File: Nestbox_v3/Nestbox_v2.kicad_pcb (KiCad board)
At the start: 2 copper layers, 85 x 60 mm, 125 parts, among them CON301 Micro_SD_Card, J201 BATT_CONN_01X02, J401 LB_DETECT_CONN_01X04, J402 CONN_01X05, J501 CONN_01X01, J502 CONN_01X06, J601 LOAD_CELL_CONN_01X04, J701 RFID_CONN_01X05, P301 RX/TX, P302 TST/RST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

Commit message: removed unnecessary footprints from PCB
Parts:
- removed CON301: Micro_SD_Card, Octanis3:MICRO-SD9+4P-SMD-16.1X14.5X1.85MM
- removed J401: LB_DETECT_CONN_01X04, Terminal_Blocks:TerminalBlock_Pheonix_MPT-2.54mm_4pol
- removed J501: CONN_01X01, Pin_Headers:Pin_Header_Straight_1x01_Pitch2.54mm
- removed JP701: V_RFID_Jumper_SELECT_Dual, Pin_Headers:Pin_Header_Straight_1x03_Pitch2.54mm
- removed Q601: DMG2301L-7 -- Replace by 0R, TO_SOT_Packages_SMD:TSOT-23
- removed Q602, Q604: DMG3402L DNP, TO_SOT_Packages_SMD:TSOT-23
- removed Q603: DMG2301L-7 DNP, TO_SOT_Packages_SMD:TSOT-23
- removed R303, R304, R305: 47R, Resistors_SMD:R_0603
- removed R401, R402, R403, R404: DNP, Resistors_SMD:R_0603
- removed R502, R613, R614, R615, R616: 82k, Resistors_SMD:R_0603
- removed R601: 1k 1% --> short with 0R, Resistors_SMD:R_0603
- removed R602: 1k 1%, Resistors_SMD:R_0603
- removed TP_RTC: CONN_01X01, Socket_Strips:Socket_Strip_Straight_1x01_Pitch2.00mm
- added J301: CONN_01X04, Pin_Headers:Pin_Header_Straight_1x04, F.Cu at (43.7, 9.91)
- added TP_RTC301: CONN_01X01, Socket_Strips:Socket_Strip_Straight_1x01_Pitch2.00mm, F.Cu at (36.7, -30.0)
- moved R507 6.11 mm to (57.7, -28.0), turned to 180 degrees
- moved Q501 2.06 mm to (57.7, -32.0), turned to 90 degrees
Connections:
- net Net-(P301-Pad1) renamed /Control/RX
- net Net-(P301-Pad2) renamed /Control/TX
- C306 pad 1: Net-(C306-Pad1) -> +3V3
- C307 pad 1: Net-(C306-Pad1) -> +3V3
- C606 pad 1: Net-(C606-Pad1) -> (no net)
- C606 pad 2: Net-(C606-Pad2) -> (no net)
- C607 pad 1: Net-(C606-Pad1) -> VAA
- C607 pad 2: Net-(C606-Pad2) -> Net-(C607-Pad2)
- J701 pad 1: /RFID/RFID_VDD -> +5V
- Q301 pad 2: Net-(C306-Pad1) -> +3V3
- Q301 pad 3: +3V3 -> Net-(J301-Pad3)
- Q501 pad 2: /Communication/ESP12_VCC -> +3V3
- Q501 pad 3: +3V3 -> /Communication/ESP12_VCC
- R605 pad 1: Net-(C606-Pad1) -> VAA
- R606 pad 1: Net-(C606-Pad2) -> Net-(C607-Pad2)
- R607 pad 2: Net-(C606-Pad2) -> Net-(C607-Pad2)
- R608 pad 2: Net-(C606-Pad1) -> VAA
- R701 pad 2: /RFID/RFID_VDD -> +5V
- U301 pad 1: /Control/LB1_LED -> /Control/RTC_CAL
- U301 pad 10: /Passage Detector/LB2_DETECT -> (no net)
- U301 pad 29: /Load_Cell/EXC_A_P -> (no net)
- U301 pad 30: /Load_Cell/EXC_A_N -> (no net)
- U301 pad 34: /Load_Cell/EXC_B_P -> (no net)
- U301 pad 35: /Load_Cell/EXC_B_N -> (no net)
- U301 pad 9: /Passage Detector/LB1_DETECT -> (no net)
- U601 pad 11: Net-(C606-Pad1) -> VAA
- U601 pad 6: Net-(C606-Pad2) -> Net-(C607-Pad2)
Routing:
- net /Load_Cell/EXC_B_P: track 81.8 -> 0.00 mm, vias 6 -> 0
- net +BATT: track 156.7 -> 80.3 mm, vias 3 -> 0
- net /Load_Cell/EXC_B_N: track 76.0 -> 0.00 mm, vias 6 -> 0
- net /Passage Detector/LB2_DETECT: track 55.4 -> 0.00 mm, vias 2 -> 0
- net /Passage Detector/LB1_DETECT: track 54.5 -> 0.00 mm, vias 2 -> 0
- net /Control/LORA_RESET_N: track 45.4 -> 0.00 mm, vias 2 -> 0
- net /Control/LB1_LED: track 43.8 -> 0.00 mm, vias 2 -> 0
- net +3V3: track 265.8 -> 235.6 mm, vias 6 -> 5
- net GND: track 249.3 -> 219.1 mm, vias 114 -> 110
- net /Load_Cell/EXC_A_P: track 27.0 -> 0.00 mm, vias 3 -> 0
- net Net-(C606-Pad1): track 25.5 -> 0.00 mm, vias 2 -> 0
- net /RFID/RFID_VDD: track 25.2 -> 0.00 mm
- net Net-(C607-Pad2): track 0.00 -> 24.3 mm, vias 0 -> 2
- net Net-(C606-Pad2): track 24.3 -> 0.00 mm, vias 2 -> 0
- net /Load_Cell/EXC_A_N: track 22.6 -> 0.00 mm, vias 2 -> 0
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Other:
- board text added: "rst tst 3V G tx rx"

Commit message: finished V3 pcb. ORDERED
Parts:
- removed C604: 10n X2Y DNP, Octanis3:Capacitor_X2Y_603
- removed C606: 10n X2Y, Octanis3:Capacitor_X2Y_603
- removed JP201: VAA_Jumper_SELECT_Dual, Pin_Headers:Pin_Header_Straight_1x03
- removed R609: 2k2, Resistors_SMD:R_0603
- added R303: 0R, Resistors_SMD:R_0603, F.Cu at (45.2, 0.75)
- added R304: 0R, Resistors_SMD:R_0603, F.Cu at (45.2, -1.50)
- R607, R608: value 0R DNP -> DNP
- moved R208 37.7 mm to (29.0, -5.50), turned to 90 degrees
- moved C202 36.3 mm to (26.5, -1.75), turned to 270 degrees
- moved TP_RTC301 33.5 mm to (15.0, -55.5)
- moved U203 31.4 mm to (25.2, -5.50), turned to 90 degrees
- moved C204 30.1 mm to (24.0, -1.75), turned to 270 degrees
- moved R610 19.2 mm to (30.5, -23.7), turned to 180 degrees
- moved REF*** 18.9 mm to (1.00, -5.00)
- moved R302 18.6 mm to (48.5, -7.50), turned to 270 degrees
- moved C601 17.8 mm to (5.94, -18.7), turned to 270 degrees
- moved R612 17.8 mm to (30.5, -13.8), turned to 180 degrees
- moved R611 17.2 mm to (30.5, -16.0), turned to 180 degrees
- moved R701 16.1 mm to (4.70, -31.0), turned to 180 degrees
- moved J601 15.8 mm to (8.48, -22.5), turned to 270 degrees
- moved J301 14.5 mm to (33.4, -0.25), turned to 90 degrees
- moved R605 14.4 mm to (11.7, -25.0), turned to 180 degrees
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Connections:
- C204 pad 1: Net-(C204-Pad1) -> VAA
- C307 pad 1: +3V3 -> Net-(C307-Pad1)
- C610 pad 2: Net-(C610-Pad2) -> VAA
- C611 pad 2: Net-(C610-Pad2) -> VAA
- J301 pad 1: /Control/TX -> Net-(J301-Pad1)
- J301 pad 2: /Control/RX -> Net-(J301-Pad2)
- J301 pad 3: Net-(J301-Pad3) -> Net-(C307-Pad1)
- Q301 pad 3: Net-(J301-Pad3) -> Net-(C307-Pad1)
- U203 pad 5: Net-(C204-Pad1) -> VAA
- U301 pad 33: /Control/LORA_RESET_N -> (no net)
- U601 pad 12: Net-(C610-Pad2) -> VAA
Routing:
- net +3V3: track 235.6 -> 171.0 mm, vias 5 -> 4
- net /Control/RTC_CAL: track 20.7 -> 59.0 mm
- net /Power/LDO_EN: track 68.8 -> 31.4 mm
- net +5V: track 83.0 -> 106.4 mm
- net /Control/SPI_MISO: track 43.3 -> 20.7 mm
- net /Load_Cell/DRDY_N: track 51.5 -> 29.7 mm, vias 0 -> 2
- net /Control/RX: track 34.8 -> 56.1 mm
- net (no net): track 20.2 -> 0.94 mm
- net /Control/SPI_MOSI: track 39.5 -> 20.7 mm
- net /Control/TX: track 35.0 -> 48.9 mm
- net Net-(J301-Pad1): track 0.00 -> 12.4 mm
- net Net-(C610-Pad2): track 11.5 -> 0.00 mm
- net Net-(C307-Pad1): track 0.00 -> 11.0 mm
- net Net-(J301-Pad2): track 0.00 -> 10.5 mm
- net /Control/RFID_DATA: track 51.0 -> 42.6 mm
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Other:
- board text added: "Digital Nestbox v3.0 by"
- board text added: "G 3V rx tx"
- board text added: "G cts 3V rx tx dtr rtc"
- board text added: "WEIGHT"
- board text added: "nestbox.octanis.org October 2018, raffael@octanis.org"
- board text added: "rtc dtr tx rx vcc cts gnd"
- board text added: "rx tx 3V G"
- board text added: "rx tx G 3V tst rst"
- board text removed: "3V3 VA reg"
- board text removed: "Digital Nestbox v2.0 by"
- board text removed: "LB_IN"
- board text removed: "VDD LB1 LB2 G"
- board text removed: "WEIGHT/ LB_OUT"
- board text removed: "bat VR 5V"
- board text removed: "dtr tx rx vcc cts gnd"
- board text removed: "nestbox.octanis.org June 2018 Tschui/Wüthrich"
- board text removed: "rst tst 3V G tx rx lora"

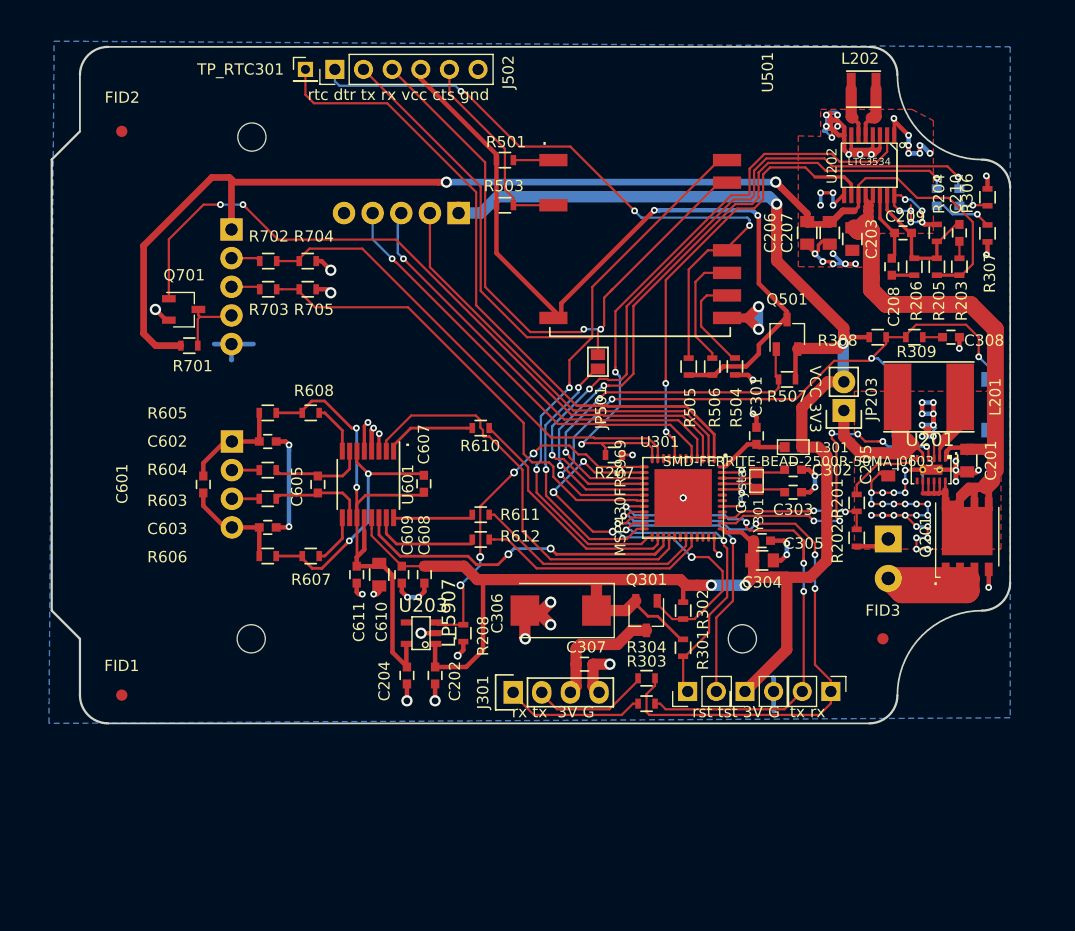
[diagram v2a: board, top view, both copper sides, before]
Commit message: exchanged both inductor footprints.
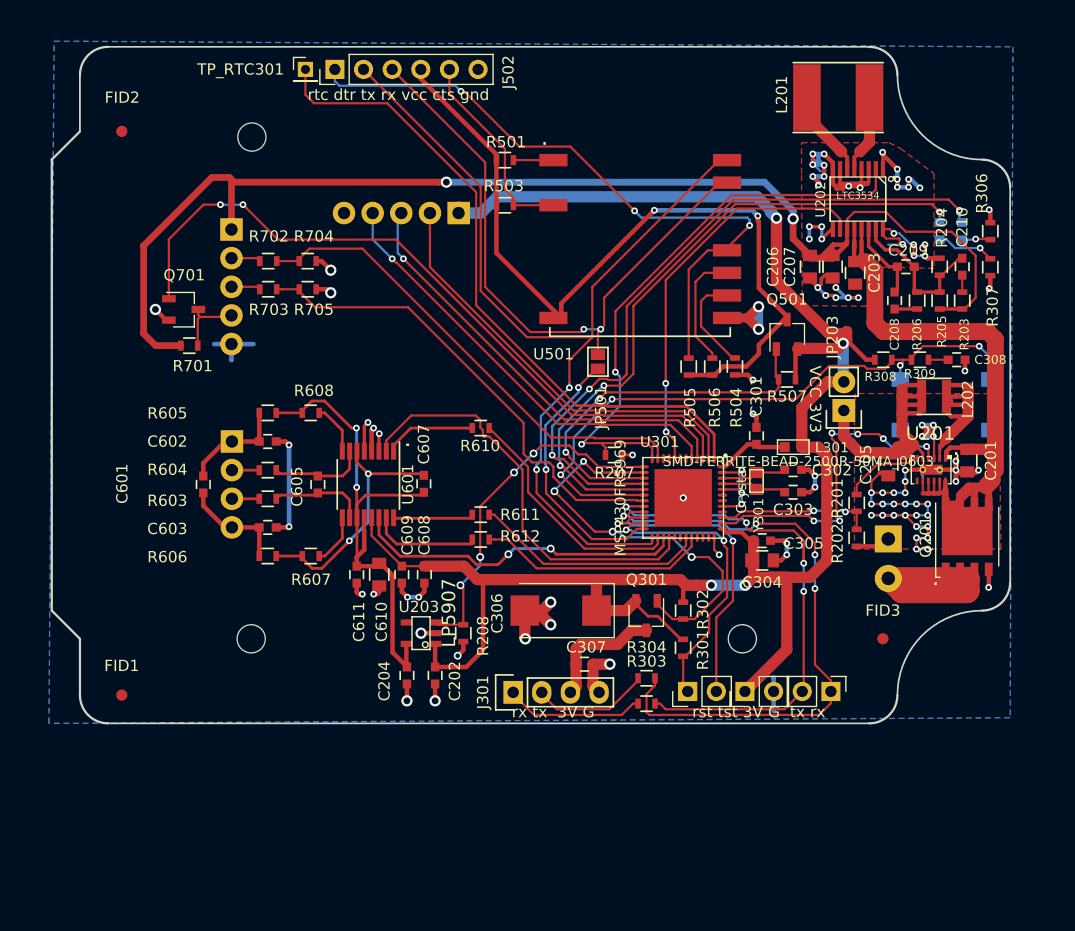
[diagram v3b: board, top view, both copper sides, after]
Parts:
- C302, C303: value 25 pF -> 24p
- C307: value 0.1u -> 100n
- L201: value 4.7uH -> 5uH
- L202: value 5uH -> 4.7uH
- Q201: value Q_PMOS_DGS -> TPH1R712MDL1Q
- Q701: value Q_NMOS_GSD -> DMG3402L
- R201: value 100k -> 82k
- R202: value 50k -> 47k
- R204: value 162k -> 162k 1%
- R205: value 649k -> 649k 1%
- R301: value 47K -> 47k
- R306, R307: value 1K -> 1k
- R308, R309, R501, R503, R504, R505, R506: value 10K -> 10k
- R604: value 1k 1% -- short to 0R -> 1k 1% --> short to 0R
- R701: value 50k -> 82k
- R702, R703: value 18k -> 47k
- R704, R705: value 33k -> 82k
- moved L202 28.0 mm to (70.8, -26.5)
- moved L201 27.7 mm to (62.2, -53.0)
- moved U202 3.16 mm to (64.0, -44.0)
- moved C203 3.01 mm to (63.8, -37.5)
- moved C206 3.01 mm to (59.8, -38.0)
- moved C207 3.01 mm to (61.8, -38.0)
- moved C208 3.01 mm to (67.2, -35.0)
- moved C209 3.01 mm to (68.2, -38.0)
- moved C210 3.01 mm to (73.2, -38.0)
- moved D301 3.01 mm to (73.2, -41.2)
- moved D302 3.01 mm to (71.2, -41.2)
- moved R203 3.01 mm to (73.2, -35.0)
- moved R204 3.01 mm to (71.2, -38.0)
- moved R205 3.01 mm to (71.2, -35.0)
- moved R206 3.01 mm to (69.2, -35.0)
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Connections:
- L201 pad 2: Net-(C205-Pad1) -> Net-(L201-Pad2)
- L202 pad 2: Net-(L202-Pad2) -> Net-(C205-Pad1)
- U201 pad 2: Net-(L201-Pad1) -> Net-(L202-Pad1)
- U202 pad 5: Net-(L202-Pad1) -> Net-(L201-Pad1)
- U202 pad 6: Net-(L202-Pad2) -> Net-(L201-Pad2)
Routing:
- net Net-(L202-Pad1): track 4.66 -> 19.2 mm
- net GND: track 211.1 -> 202.1 mm, vias 106 -> 103
- net +BATT: track 80.3 -> 71.5 mm
- net Net-(L201-Pad2): track 0.00 -> 7.85 mm
- net +5V: track 106.4 -> 112.9 mm
- net Net-(L202-Pad2): track 4.39 -> 0.00 mm
- net /Power/5V_PWM: track 39.7 -> 35.5 mm
- net Net-(C205-Pad1): track 24.1 -> 28.1 mm
- net /Control/5V_ENABLE: track 55.3 -> 51.4 mm
- net /Control/DBG_Switch: track 60.4 -> 56.9 mm
- net +3V3: track 171.0 -> 174.2 mm
- net /Control/DBG_LED2: track 61.1 -> 58.3 mm
- net /Control/DBG_LED1: track 64.3 -> 61.5 mm
- net Net-(C209-Pad1): track 12.8 -> 14.0 mm
- net Net-(C208-Pad2): track 6.24 -> 7.21 mm
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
